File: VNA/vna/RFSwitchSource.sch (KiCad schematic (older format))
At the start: 2 parts

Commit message: finished controller, chose compatible switches
controller and rf switches have been completed.

ToDo: finish filter design for RF Source, add auto gain control
ToDo: finish directional coupler footprints
ToDo: PCB Layout
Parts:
- removed SWs1: ADG918BRM, Package_SO:MSOP-8_3x3mm_P0.65mm, symbol RF_Switch:ADG918BRM
- added C2, C3: 100n, Capacitor_SMD:C_0805_2012Metric_Pad1.15x1.40mm_HandSolder, symbol Device:C_Small
- added U1: 74HCT04, Package_SO:SOIC-14_3.9x8.7mm_P1.27mm, symbol 74xx:74HCT04
- added U2: HMC284, Package_SO:MSOP-8-1EP_3x3mm_P0.65mm_EP2.5x3mm_Mask1.73x2.36mm_ThermalVias, symbol vna-rescue:HMC284
- C1: value 10u -> 100n; footprint (none) -> Capacitor_SMD:C_0805_2012Metric_Pad1.15x1.40mm_HandSolder
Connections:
- net labels added: GND
- net labels removed: GNDD, VDD
- wire segments 6 -> 20
- no-connect marks 0 -> 1
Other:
- note added: "Hex Inverter"
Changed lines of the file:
@@
 Comment4 ""
 $EndDescr
+Text HLabel 3150 3400 0    50   Input ~ 0
+Ctrl
+Text HLabel 4250 1500 0    50   Input ~ 0
+SrcOutB
+Text HLabel 5250 1500 2    50   Input ~ 0
+SrcOutA
+Text HLabel 4900 3600 3    50   Input ~ 0
+SrcIn
 $Comp
-L RF_Switch:ADG918BRM SWs?
-U 1 1 5CC6F338
-P 5150 2750
-AR Path="/5CC6F338" Ref="SWs?"  Part="1"
-AR Path="/5CC6DDE1/5CC6F338" Ref="SWs1"  Part="1"
-AR Path="/5CCA83E4/5CC6F338" Ref="SWs?"  Part="1"
-AR Path="/5CCA873A/5CC6F338" Ref="SWs?"  Part="1"
-F 0 "SWs1" H 4900 3100 50  0000 C CNN
-F 1 "ADG918BRM" H 5400 3200 50  0000 C CNN
-F 2 "Package_SO:MSOP-8_3x3mm_P0.65mm" H 5150 2300 50  0001 C CNN
-F 3 "https://www.analog.com/media/en/technical-documentation/data-sheets/ADG918_919.pdf" H 5100 2950 50  0001 C CNN
-	1    5150 2750
+L vna-rescue:HMC284 U2
+U 1 1 5D841F80
+P 4800 2650
+F 0 "U2" H 5178 2721 50  0000 L CNN
+F 1 "HMC284" H 5178 2630 50  0000 L CNN
+F 2 "Package_SO:MSOP-8-1EP_3x3mm_P0.65mm_EP2.5x3mm_Mask1.73x2.36mm_ThermalVias" H 4550 2700 50  0001 C CNN
+F 3 "" H 4550 2700 50  0001 C CNN
+	1    4800 2650
 	1    0    0    -1
 $EndComp
 $Comp
-L Device:C_Small C?
-U 1 1 5CC702A7
-P 6400 2600
-AR Path="/5CC702A7" Ref="C?"  Part="1"
-AR Path="/5CC6DDE1/5CC702A7" Ref="C1"  Part="1"
-AR Path="/5CCA83E4/5CC702A7" Ref="C?"  Part="1"
-AR Path="/5CCA873A/5CC702A7" Ref="C?"  Part="1"
-F 0 "C1" H 6492 2646 50  0000 L CNN
-F 1 "10u" H 6492 2555 50  0000 L CNN
-F 2 "" H 6400 2600 50  0001 C CNN
-F 3 "~" H 6400 2600 50  0001 C CNN
-	1    6400 2600
+L power:GND #PWR016
+U 1 1 5D843902
+P 4800 1900
+F 0 "#PWR016" H 4800 1650 50  0001 C CNN
+F 1 "GND" H 4805 1727 50  0000 C CNN
+F 2 "" H 4800 1900 50  0001 C CNN
+F 3 "" H 4800 1900 50  0001 C CNN
+	1    4800 1900
 	1    0    0    -1
 $EndComp
-Text HLabel 4650 2650 0    50   Input ~ 0
-SrcIn
-Text HLabel 5650 2550 2    50   Input ~ 0
-SrcOutA
-Text HLabel 5650 2750 2    50   Input ~ 0
-SrcOutB
+Wire Wire Line
+	4700 2100 4700 1900
+Wire Wire Line
+	4700 1900 4800 1900
+Wire Wire Line
+	4800 1900 4900 1900
+Wire Wire Line
+	4900 1900 4900 2100
+Connection ~ 4800 1900
+NoConn ~ 5050 3150
 $Comp
-L power:GNDD #PWR012
-U 1 1 5CCA53F1
-P 5150 3300
-AR Path="/5CC6DDE1/5CCA53F1" Ref="#PWR012"  Part="1"
-AR Path="/5CCA83E4/5CCA53F1" Ref="#PWR?"  Part="1"
-AR Path="/5CCA873A/5CCA53F1" Ref="#PWR?"  Part="1"
-F 0 "#PWR012" H 5150 3050 50  0001 C CNN
-F 1 "GNDD" H 5154 3145 50  0000 C CNN
-F 2 "" H 5150 3300 50  0001 C CNN
-F 3 "" H 5150 3300 50  0001 C CNN
-	1    5150 3300
+L Device:C_Small C3
+U 1 1 5D84B78C
+P 4900 3350
+F 0 "C3" H 4992 3396 50  0000 L CNN
+F 1 "100n" H 4992 3305 50  0000 L CNN
+F 2 "Capacitor_SMD:C_0805_2012Metric_Pad1.15x1.40mm_HandSolder" H 4900 3350 50  0001 C CNN
+F 3 "~" H 4900 3350 50  0001 C CNN
+	1    4900 3350
+	1    0    0    -1
+$EndComp
+Wire Wire Line
+	4900 3150 4900 3250
+Wire Wire Line
+	4900 3450 4900 3600
+$Comp
+L Device:C_Small C1
+U 1 1 5D84E6D7
+P 4250 1800
+F 0 "C1" H 4342 1846 50  0000 L CNN
+F 1 "100n" H 4342 1755 50  0000 L CNN
+F 2 "Capacitor_SMD:C_0805_2012Metric_Pad1.15x1.40mm_HandSolder" H 4250 1800 50  0001 C CNN
+F 3 "~" H 4250 1800 50  0001 C CNN
+	1    4250 1800
 	1    0    0    -1
 $EndComp
 $Comp
-L power:VDD #PWR011
-U 1 1 5CCA5AC1
-P 5150 2200
-AR Path="/5CC6DDE1/5CCA5AC1" Ref="#PWR011"  Part="1"
-AR Path="/5CCA83E4/5CCA5AC1" Ref="#PWR?"  Part="1"
-AR Path="/5CCA873A/5CCA5AC1" Ref="#PWR?"  Part="1"
-F 0 "#PWR011" H 5150 2050 50  0001 C CNN
-F 1 "VDD" H 5167 2373 50  0000 C CNN
-F 2 "" H 5150 2200 50  0001 C CNN
-F 3 "" H 5150 2200 50  0001 C CNN
-	1    5150 2200
+L Device:C_Small C2
+U 1 1 5D84EC63
+P 5250 1800
+F 0 "C2" H 5342 1846 50  0000 L CNN
+F 1 "100n" H 5342 1755 50  0000 L CNN
+F 2 "Capacitor_SMD:C_0805_2012Metric_Pad1.15x1.40mm_HandSolder" H 5250 1800 50  0001 C CNN
+F 3 "~" H 5250 1800 50  0001 C CNN
+	1    5250 1800
 	1    0    0    -1
 $EndComp
-Text HLabel 4650 2850 0    50   Input ~ 0
-Ctrl
 Wire Wire Line
-	5150 2200 6400 2200
+	5050 2100 5250 2100
 Wire Wire Line
-	6400 2200 6400 2500
+	5250 2100 5250 1900
 Wire Wire Line
-	5150 2200 5150 2250
-Connection ~ 5150 2200
+	4550 2100 4250 2100
 Wire Wire Line
-	5150 3250 5150 3300
+	4250 2100 4250 1900
 Wire Wire Line
-	5150 3300 6400 3300
+	5250 1700 5250 1500
 Wire Wire Line
-	6400 2700 6400 3300
-Connection ~ 5150 3300
-Text GLabel 5800 2200 1    50   Input ~ 0
-VDD
-Text GLabel 5800 3300 3    50   Input ~ 0
-GNDD
+	4250 1700 4250 1500
+$Comp
+L 74xx:74HCT04 U1
+U 1 1 5D84F697
+P 3650 3400
+F 0 "U1" H 3650 3250 50  0000 C CNN
+F 1 "74HCT04" H 3650 3150 50  0000 C CNN
+F 2 "Package_SO:SOIC-14_3.9x8.7mm_P1.27mm" H 3650 3400 50  0001 C CNN
+F 3 "https://assets.nexperia.com/documents/data-sheet/74HC_HCT04.pdf" H 3650 3400 50  0001 C CNN
+	1    3650 3400
+	1    0    0    -1
+$EndComp
+$Comp
+L 74xx:74HCT04 U1
+U 2 1 5D852517
+P 4300 4050
+F 0 "U1" H 4300 4367 50  0000 C CNN
+F 1 "74HCT04" H 4300 4276 50  0000 C CNN
+F 2 "Package_SO:SOIC-14_3.9x8.7mm_P1.27mm" H 4300 4050 50  0001 C CNN
+F 3 "https://assets.nexperia.com/documents/data-sheet/74HC_HCT04.pdf" H 4300 4050 50  0001 C CNN
+	2    4300 4050
+	1    0    0    -1
+$EndComp
+Wire Wire Line
+	3950 3400 3950 3650
+Wire Wire Line
+	3950 4050 4000 4050
+Wire Wire Line
+	3950 3650 4550 3650
+Wire Wire Line
+	4550 3650 4550 3150
+Connection ~ 3950 3650
+Wire Wire Line
+	3950 3650 3950 4050
+Wire Wire Line
+	4600 4050 4700 4050
+Wire Wire Line
+	4700 4050 4700 3150
+Wire Wire Line
+	3150 3400 3350 3400
+Text Notes 3350 3900 0    50   ~ 0
+Hex Inverter
+Wire Notes Line
+	3250 3200 3250 4300
+Wire Notes Line
+	3250 4300 4800 4300
+Wire Notes Line
+	4800 4300 4800 3200
+Wire Notes Line
+	4800 3200 3250 3200
 $EndSCHEMATC

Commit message: custom footprint for couplers, added decoupling caps
added custom footprint for directional couplers - will need to verify it

added decoupling caps to ad9851
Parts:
- C1, C2, C3: footprint Capacitor_SMD:C_0805_2012Metric_Pad1.15x1.40mm_HandSolder -> Capacitor_SMD:C_1206_3216Metric_Pad1.42x1.75mm_HandSolder
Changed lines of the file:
@@
 $Descr A4 11693 8268
 encoding utf-8
-Sheet 4 10
+Sheet 3 10
 Title ""
 Date ""
@@
 F 0 "C3" H 4992 3396 50  0000 L CNN
 F 1 "100n" H 4992 3305 50  0000 L CNN
-F 2 "Capacitor_SMD:C_0805_2012Metric_Pad1.15x1.40mm_HandSolder" H 4900 3350 50  0001 C CNN
+F 2 "Capacitor_SMD:C_1206_3216Metric_Pad1.42x1.75mm_HandSolder" H 4900 3350 50  0001 C CNN
 F 3 "~" H 4900 3350 50  0001 C CNN
 	1    4900 3350
@@
 F 0 "C1" H 4342 1846 50  0000 L CNN
 F 1 "100n" H 4342 1755 50  0000 L CNN
-F 2 "Capacitor_SMD:C_0805_2012Metric_Pad1.15x1.40mm_HandSolder" H 4250 1800 50  0001 C CNN
+F 2 "Capacitor_SMD:C_1206_3216Metric_Pad1.42x1.75mm_HandSolder" H 4250 1800 50  0001 C CNN
 F 3 "~" H 4250 1800 50  0001 C CNN
 	1    4250 1800
@@
 F 0 "C2" H 5342 1846 50  0000 L CNN
 F 1 "100n" H 5342 1755 50  0000 L CNN
-F 2 "Capacitor_SMD:C_0805_2012Metric_Pad1.15x1.40mm_HandSolder" H 5250 1800 50  0001 C CNN
+F 2 "Capacitor_SMD:C_1206_3216Metric_Pad1.42x1.75mm_HandSolder" H 5250 1800 50  0001 C CNN
 F 3 "~" H 5250 1800 50  0001 C CNN
 	1    5250 1800

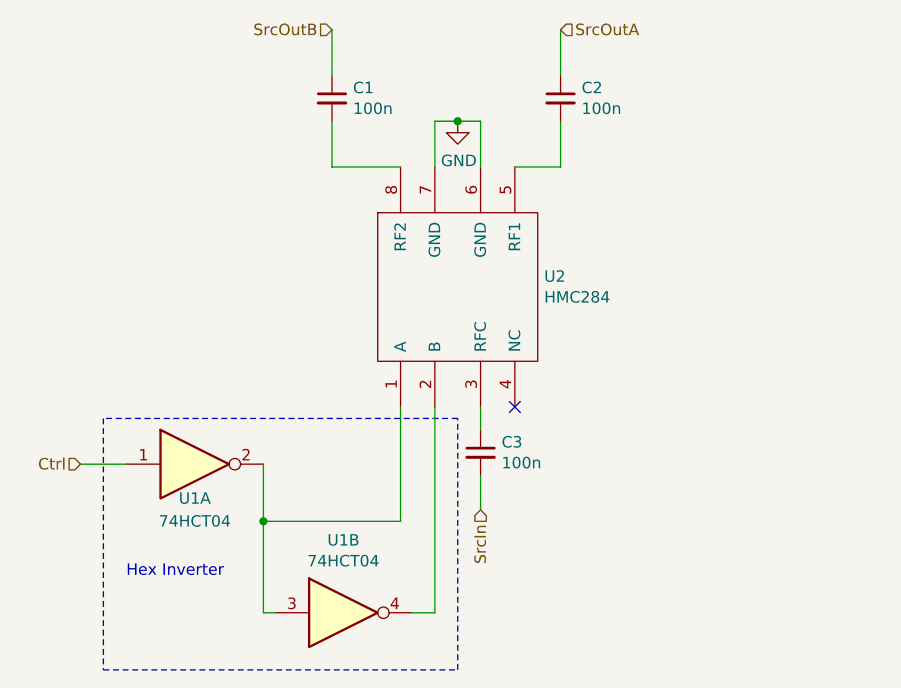
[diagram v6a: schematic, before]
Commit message: initial pcb design
initial layout and grouping of components complete
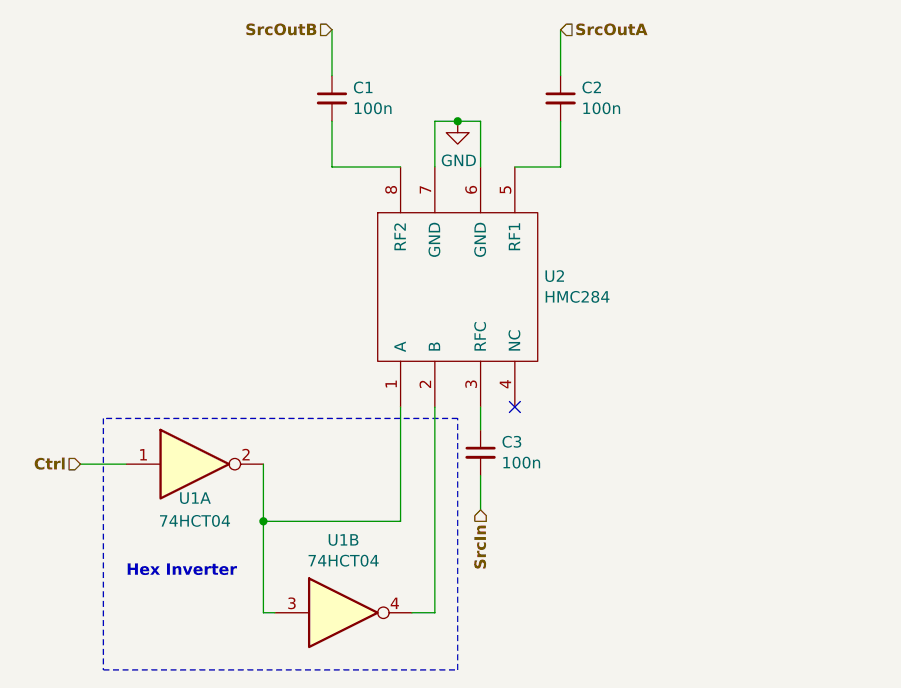
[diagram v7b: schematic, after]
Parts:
- C1, C2, C3: footprint Capacitor_SMD:C_1206_3216Metric_Pad1.42x1.75mm_HandSolder -> Capacitor_SMD:C_0805_2012Metric_Pad1.15x1.40mm_HandSolder
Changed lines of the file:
@@
 encoding utf-8
 Sheet 3 10
-Title ""
-Date ""
-Rev ""
-Comp ""
+Title "RF Source Switch"
+Date "2019-09-25"
+Rev "0.1"
+Comp "Benjamin Jackson"
 Comment1 ""
 Comment2 ""
@@
 Comment4 ""
 $EndDescr
-Text HLabel 3150 3400 0    50   Input ~ 0
+Text HLabel 3150 3400 0    50   Input ~ 10
 Ctrl
-Text HLabel 4250 1500 0    50   Input ~ 0
+Text HLabel 4250 1500 0    50   Input ~ 10
 SrcOutB
-Text HLabel 5250 1500 2    50   Input ~ 0
+Text HLabel 5250 1500 2    50   Input ~ 10
 SrcOutA
-Text HLabel 4900 3600 3    50   Input ~ 0
+Text HLabel 4900 3600 3    50   Input ~ 10
 SrcIn
 $Comp
@@
 F 0 "C3" H 4992 3396 50  0000 L CNN
 F 1 "100n" H 4992 3305 50  0000 L CNN
-F 2 "Capacitor_SMD:C_1206_3216Metric_Pad1.42x1.75mm_HandSolder" H 4900 3350 50  0001 C CNN
+F 2 "Capacitor_SMD:C_0805_2012Metric_Pad1.15x1.40mm_HandSolder" H 4900 3350 50  0001 C CNN
 F 3 "~" H 4900 3350 50  0001 C CNN
 	1    4900 3350
@@
 F 0 "C1" H 4342 1846 50  0000 L CNN
 F 1 "100n" H 4342 1755 50  0000 L CNN
-F 2 "Capacitor_SMD:C_1206_3216Metric_Pad1.42x1.75mm_HandSolder" H 4250 1800 50  0001 C CNN
+F 2 "Capacitor_SMD:C_0805_2012Metric_Pad1.15x1.40mm_HandSolder" H 4250 1800 50  0001 C CNN
 F 3 "~" H 4250 1800 50  0001 C CNN
 	1    4250 1800
@@
 F 0 "C2" H 5342 1846 50  0000 L CNN
 F 1 "100n" H 5342 1755 50  0000 L CNN
-F 2 "Capacitor_SMD:C_1206_3216Metric_Pad1.42x1.75mm_HandSolder" H 5250 1800 50  0001 C CNN
+F 2 "Capacitor_SMD:C_0805_2012Metric_Pad1.15x1.40mm_HandSolder" H 5250 1800 50  0001 C CNN
 F 3 "~" H 5250 1800 50  0001 C CNN
 	1    5250 1800
@@
 Wire Wire Line
 	3150 3400 3350 3400
-Text Notes 3350 3900 0    50   ~ 0
+Text Notes 3350 3900 0    50   ~ 10
 Hex Inverter
 Wire Notes Line

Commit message: v0.1 completed, producing gerbers
gerbers to be sent to jlc pcb pending their acceptance, they will be produced
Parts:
- U1: footprint Package_SO:SOIC-14_3.9x8.7mm_P1.27mm -> Package_DIP:DIP-14_W10.16mm
- U2: footprint Package_SO:MSOP-8-1EP_3x3mm_P0.65mm_EP2.5x3mm_Mask1.73x2.36mm_ThermalVias -> Package_SO:MSOP-8-1EP_3x3mm_P0.65mm_EP2.5x3mm_Mask1.73x2.36mm
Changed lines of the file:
@@
 F 0 "U2" H 5178 2721 50  0000 L CNN
 F 1 "HMC284" H 5178 2630 50  0000 L CNN
-F 2 "Package_SO:MSOP-8-1EP_3x3mm_P0.65mm_EP2.5x3mm_Mask1.73x2.36mm_ThermalVias" H 4550 2700 50  0001 C CNN
+F 2 "Package_SO:MSOP-8-1EP_3x3mm_P0.65mm_EP2.5x3mm_Mask1.73x2.36mm" H 4550 2700 50  0001 C CNN
 F 3 "" H 4550 2700 50  0001 C CNN
 	1    4800 2650
@@
 F 0 "U1" H 3650 3250 50  0000 C CNN
 F 1 "74HCT04" H 3650 3150 50  0000 C CNN
-F 2 "Package_SO:SOIC-14_3.9x8.7mm_P1.27mm" H 3650 3400 50  0001 C CNN
+F 2 "Package_DIP:DIP-14_W10.16mm" H 3650 3400 50  0001 C CNN
 F 3 "https://assets.nexperia.com/documents/data-sheet/74HC_HCT04.pdf" H 3650 3400 50  0001 C CNN
 	1    3650 3400
@@
 F 0 "U1" H 4300 4367 50  0000 C CNN
 F 1 "74HCT04" H 4300 4276 50  0000 C CNN
-F 2 "Package_SO:SOIC-14_3.9x8.7mm_P1.27mm" H 4300 4050 50  0001 C CNN
+F 2 "Package_DIP:DIP-14_W10.16mm" H 4300 4050 50  0001 C CNN
 F 3 "https://assets.nexperia.com/documents/data-sheet/74HC_HCT04.pdf" H 4300 4050 50  0001 C CNN
 	2    4300 4050
@@
 $EndComp
 Wire Wire Line
-	3950 3400 3950 3650
-Wire Wire Line
 	3950 4050 4000 4050
-Wire Wire Line
-	3950 3650 4550 3650
-Wire Wire Line
-	4550 3650 4550 3150
-Connection ~ 3950 3650
-Wire Wire Line
-	3950 3650 3950 4050
-Wire Wire Line
-	4600 4050 4700 4050
-Wire Wire Line
-	4700 4050 4700 3150
 Wire Wire Line
 	3150 3400 3350 3400
@@
 Wire Notes Line
 	4800 3200 3250 3200
+Wire Wire Line
+	4700 4050 4700 3150
+Wire Wire Line
+	4600 4050 4700 4050
+Wire Wire Line
+	3950 3400 3950 3650
+Wire Wire Line
+	3950 3650 3950 4050
+Connection ~ 3950 3650
+Wire Wire Line
+	3950 3650 4550 3650
+Wire Wire Line
+	4550 3650 4550 3150
 $EndSCHEMATC
